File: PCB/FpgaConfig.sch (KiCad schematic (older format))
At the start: 6 parts, among them J5 TSM-105-01-S-DV, U4 S25FL128SAGMFI000, U5 10CLxxxYE144, X1 SG-5032CAN

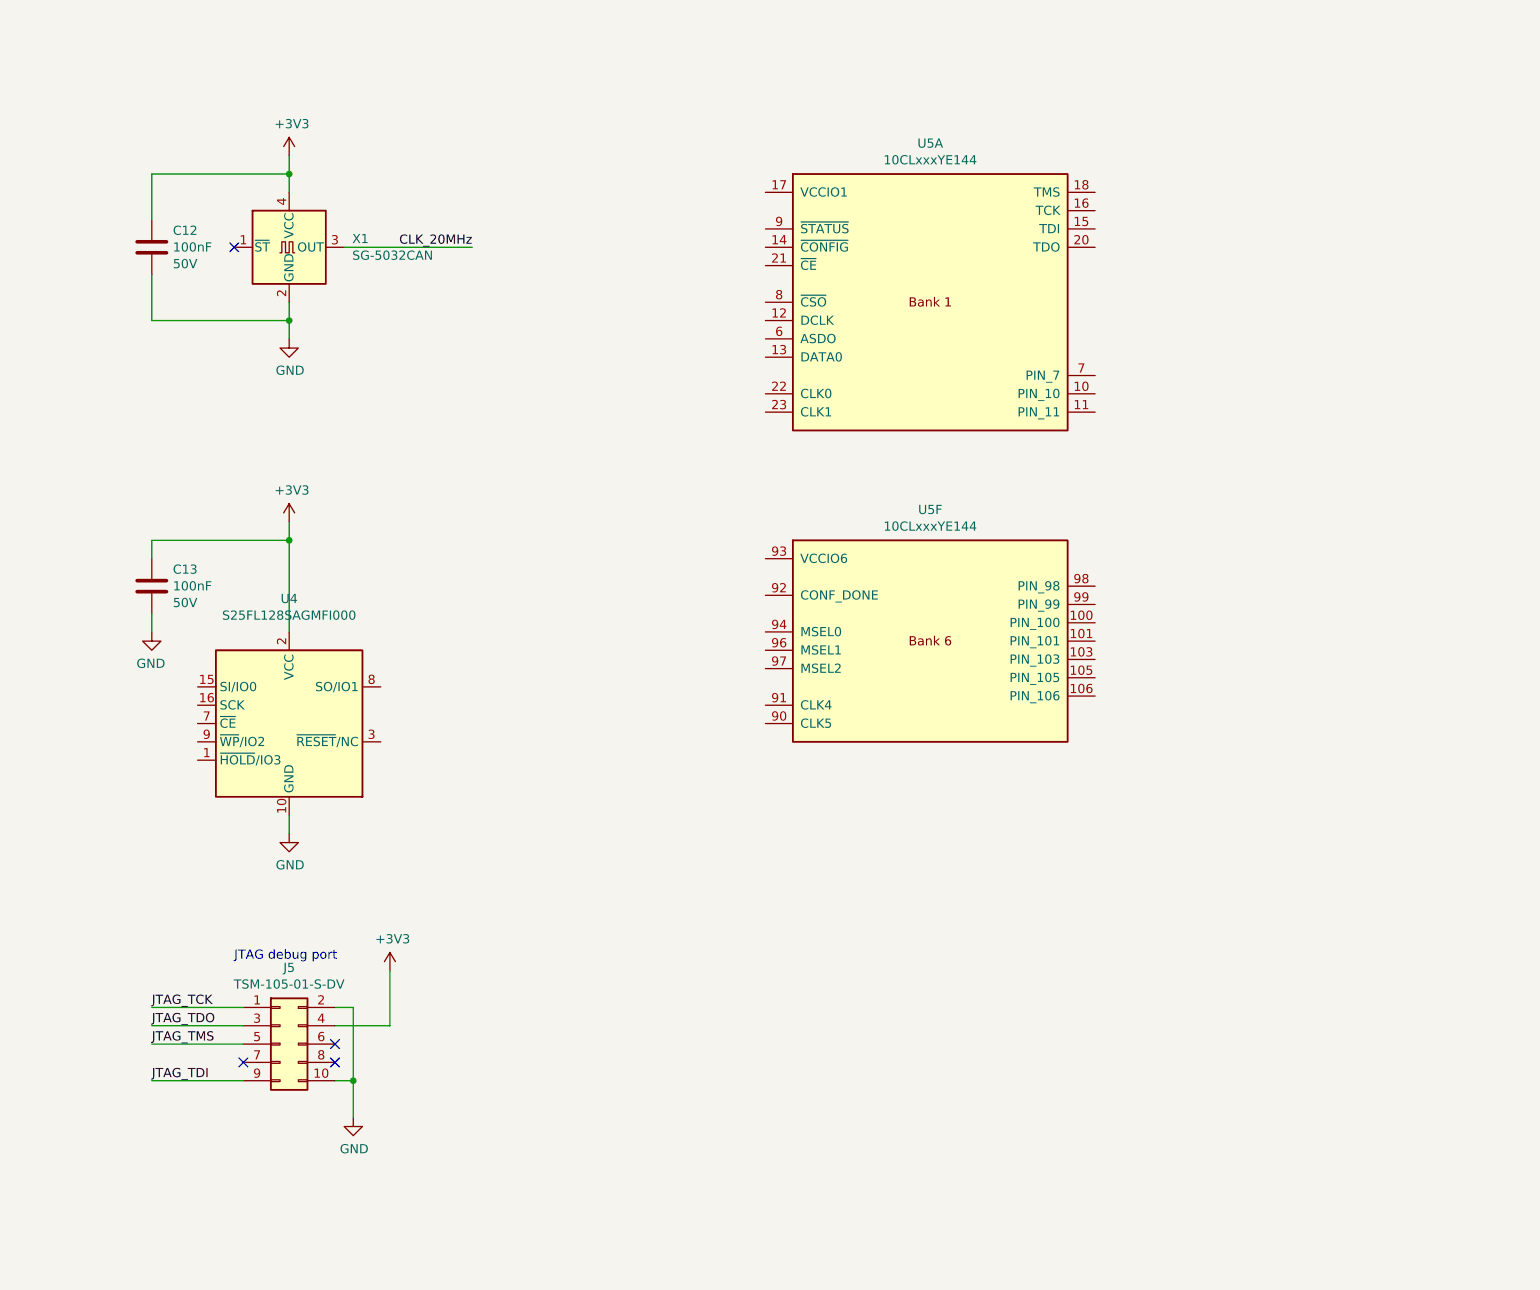
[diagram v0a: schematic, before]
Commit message: Connect the FPGA configuration signals
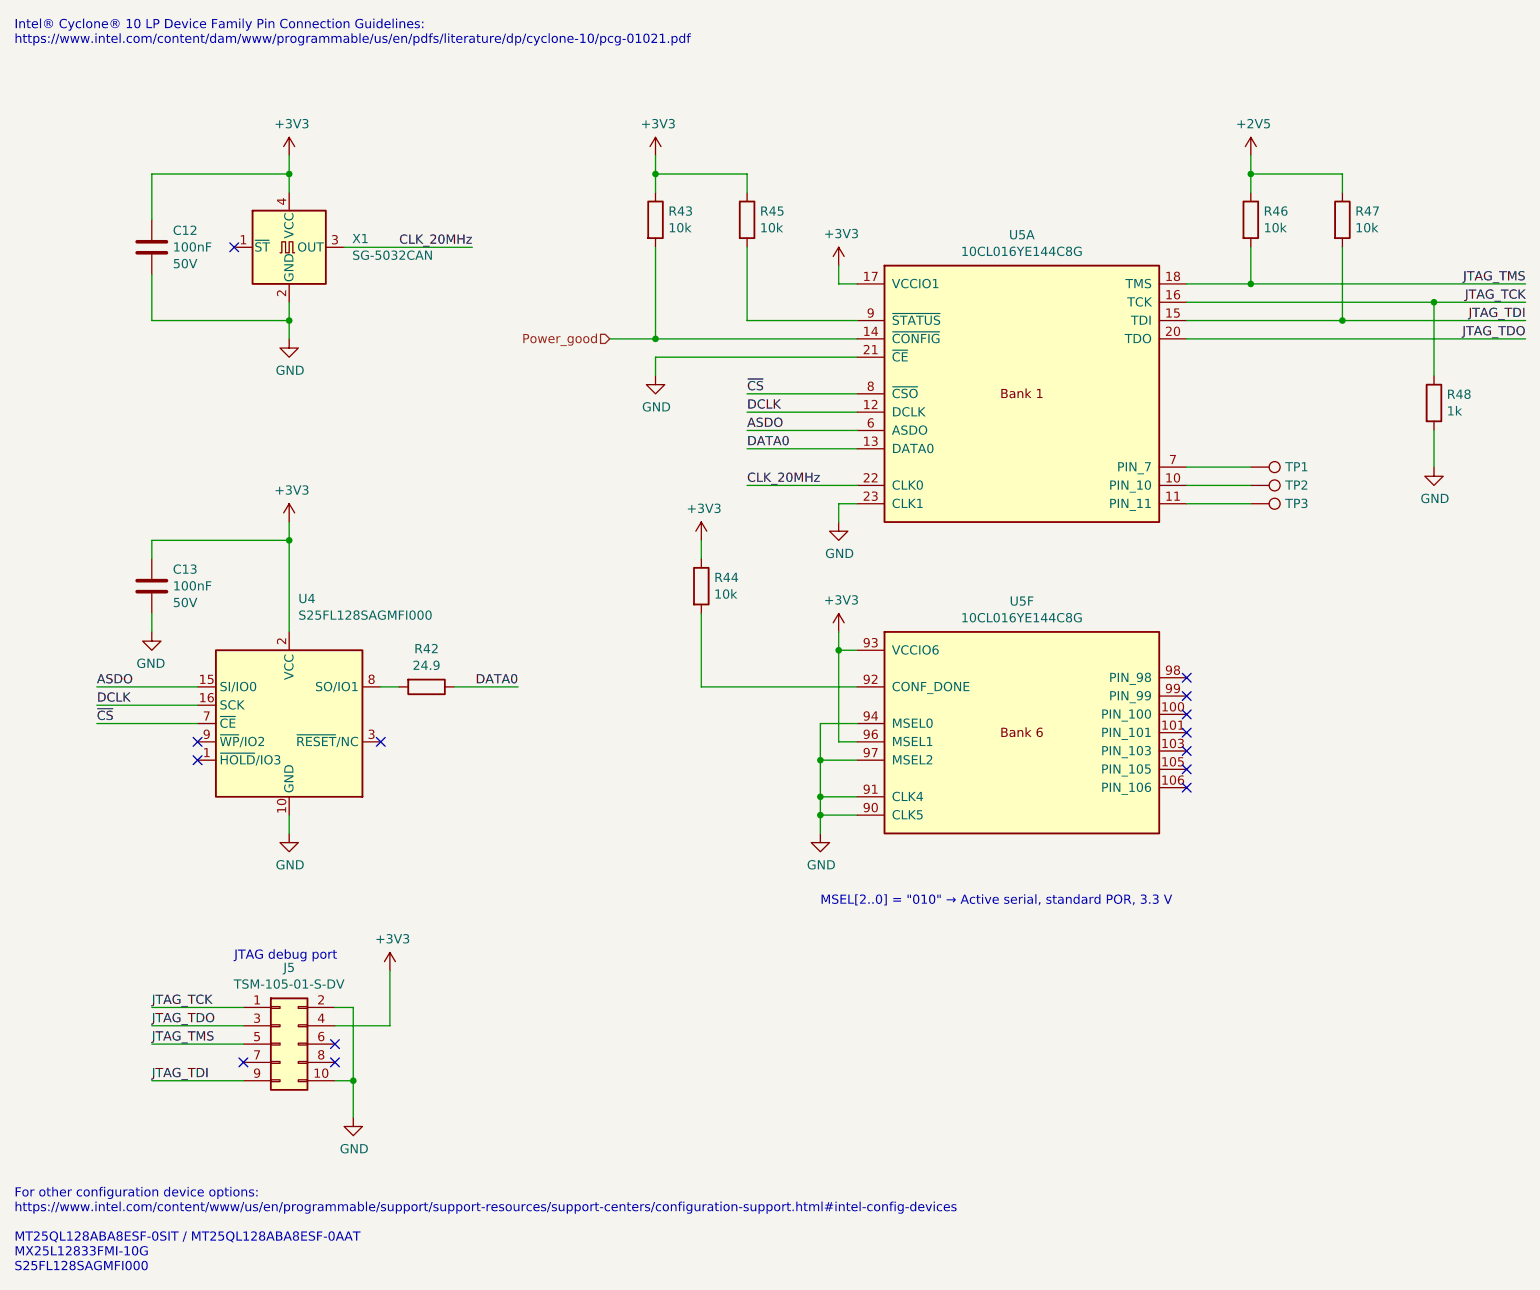
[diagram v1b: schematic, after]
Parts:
- added R42: 24.9, Resistor_SMD:R_0603_1608Metric, symbol Device:R
- added R43, R44, R45, R46, R47: 10k, Resistor_SMD:R_0603_1608Metric, symbol Device:R
- added R48: 1k, Resistor_SMD:R_0603_1608Metric, symbol Device:R
- added TP1, TP2, TP3: TestPoint, TestPoint:TestPoint_Pad_D1.0mm, symbol Connector:TestPoint
- C12, C13: Part_Number C1608X5R1H104K080AA -> (none); Part_number (none) -> C1608X5R1H104K080AA
- U5: value 10CLxxxYE144 -> 10CL016YE144C8G; Part_number (none) -> 10CL016YE144C8G
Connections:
- net +3V3: now also U5.17 (VCCIO1), U5.93 (VCCIO6), U5.96 (MSEL1), R43.1, R44.1, R45.1
- net CLK_20MHz: now also U5.22 (CLK0)
- net GND: now also U5.21 (~CE), U5.23 (CLK1), U5.90 (CLK5), U5.91 (CLK4), U5.94 (MSEL0), U5.97 (MSEL2), R48.2
- net JTAG_TCK: now also U5.16 (TCK), R48.1
- net JTAG_TDI: now also U5.15 (TDI), R47.2
- net JTAG_TDO: now also U5.20 (TDO)
- net JTAG_TMS: now also U5.18 (TMS), R46.2
- net at U5.10 (PIN_10): now also TP2.1
- net at U5.11 (PIN_11): now also TP3.1
- net DCLK: now reaches U5.12 (DCLK)
- net DCLK: now also U4.16 (SCK)
- net DATA0: now reaches U5.13 (DATA0)
- net DATA0: now also R42.1
- net Power_good: now reaches U5.14 (~CONFIG)
- net Power_good: now also R43.2
- net ASDO: now reaches U5.6 (ASDO)
- net ASDO: now also U4.15 (SI/IO0)
- net at U5.7 (PIN_7): now also TP1.1
- net ~CS: now reaches U5.8 (~CSO)
- net ~CS: now also U4.7 (~CE)
- net at U5.9 (~STATUS): now also R45.2
- net at U4.8 (SO/IO1): now also R42.2
- net at U5.92 (CONF_DONE): now also R44.2
- new net +2V5: R46.1, R47.1
- no-connect marks 4 -> 14
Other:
- note added: "For other configuration device options:\nhttps://www.intel.com/content/www/us/en/programmable/support/support-resources/support-centers/configuration-support.html#intel-config-devices\n\nMT25QL128ABA8ESF-0SIT / MT25QL128ABA8ESF-0AAT\nMX25L12833FMI-10G\nS25FL128SAGMFI000"
- note added: "Intel® Cyclone® 10 LP Device Family Pin Connection Guidelines:\nhttps://www.intel.com/content/dam/www/programmable/us/en/pdfs/literature/dp/cyclone-10/pcg-01021.pdf"
- note added: "MSEL[2..0] = "010" → Active serial, standard POR, 3.3 V"
- moved on the sheet: U5A, U5F
